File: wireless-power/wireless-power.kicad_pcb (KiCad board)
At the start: 2 copper layers, 82 x 40.6 mm, 16 parts, among them J1 Screw_Terminal_01x01, J2 Screw_Terminal_01x01, Q1 BD139, U1 TPS62112RSAR, U2 NE555DR

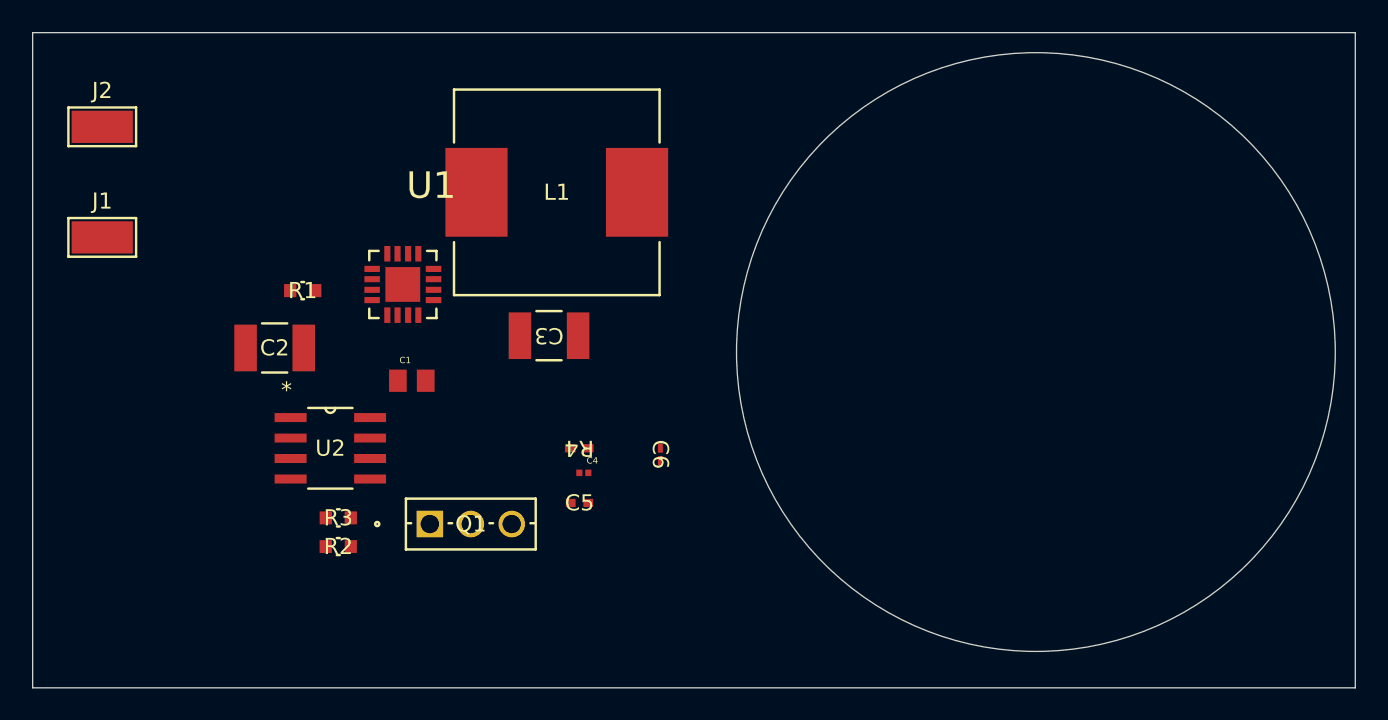
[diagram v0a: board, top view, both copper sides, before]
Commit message: preliminary layout
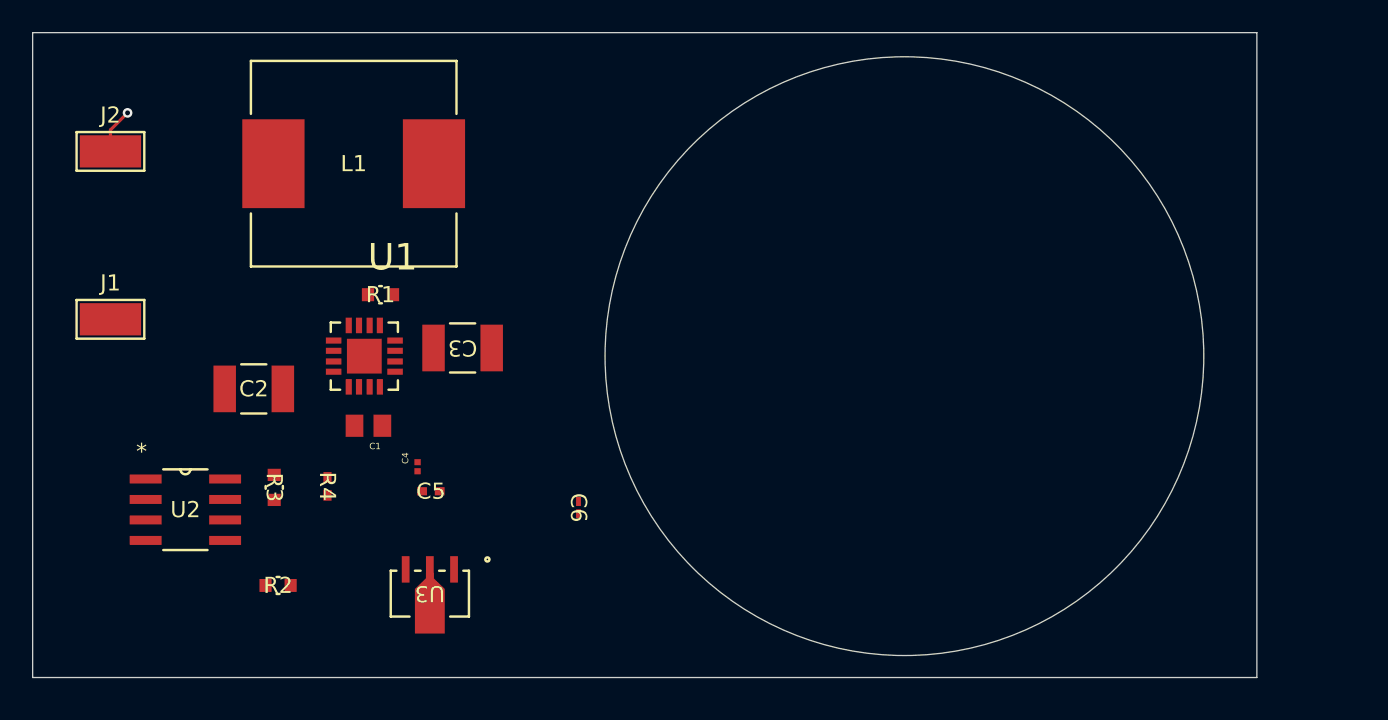
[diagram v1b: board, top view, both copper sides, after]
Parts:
- removed Q1: BD139, wireless-power-footprints:SOT-32_STM
- added U3: PBSS4480X, wireless-power-footprints:SOT89_NXP, F.Cu at (135.9, 91.7)
- moved R4 15.8 mm to (129.5, 85.0), turned to -90 degrees
- moved L1 12.7 mm to (131.2, 65.0)
- moved C4 10.3 mm to (135.1, 83.8), turned to 90 degrees
- moved U2 9.77 mm to (120.7, 86.5)
- moved C5 9.25 mm to (136.0, 85.3)
- moved C6 6.06 mm to (145.1, 86.4)
- moved C3 5.41 mm to (137.9, 76.5)
- moved J1 5.11 mm to (116.1, 74.7)
- moved U1 5.05 mm to (131.8, 77.0)
- moved R1 4.83 mm to (132.8, 73.2)
- moved R2 4.45 mm to (126.5, 91.2)
- moved R3 4.40 mm to (126.2, 85.1), turned to -90 degrees
- moved C1 3.88 mm to (132.1, 81.3), turned to 180 degrees
- moved C2 2.85 mm to (125.0, 79.0)
- moved J2 1.61 mm to (116.1, 64.3)
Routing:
- net GND: track 0.00 -> 2.83 mm, vias 0 -> 1
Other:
- board size 82 x 40.6 mm -> 75.9 x 40 mm

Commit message: routed traces
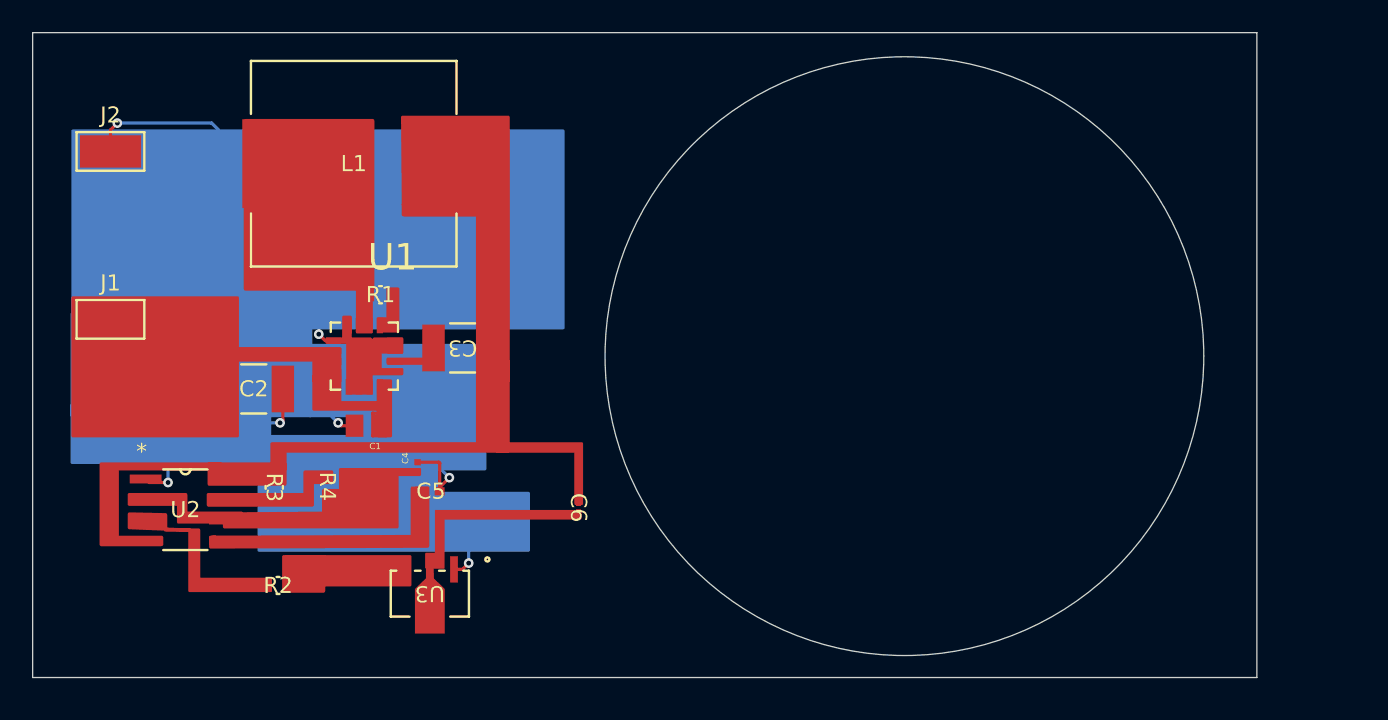
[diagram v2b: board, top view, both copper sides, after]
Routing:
- net GND: track 2.83 -> 78.1 mm, vias 1 -> 7
- net /+5V: track 0.00 -> 5.26 mm
